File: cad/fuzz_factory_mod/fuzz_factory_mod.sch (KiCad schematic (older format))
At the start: 2 parts

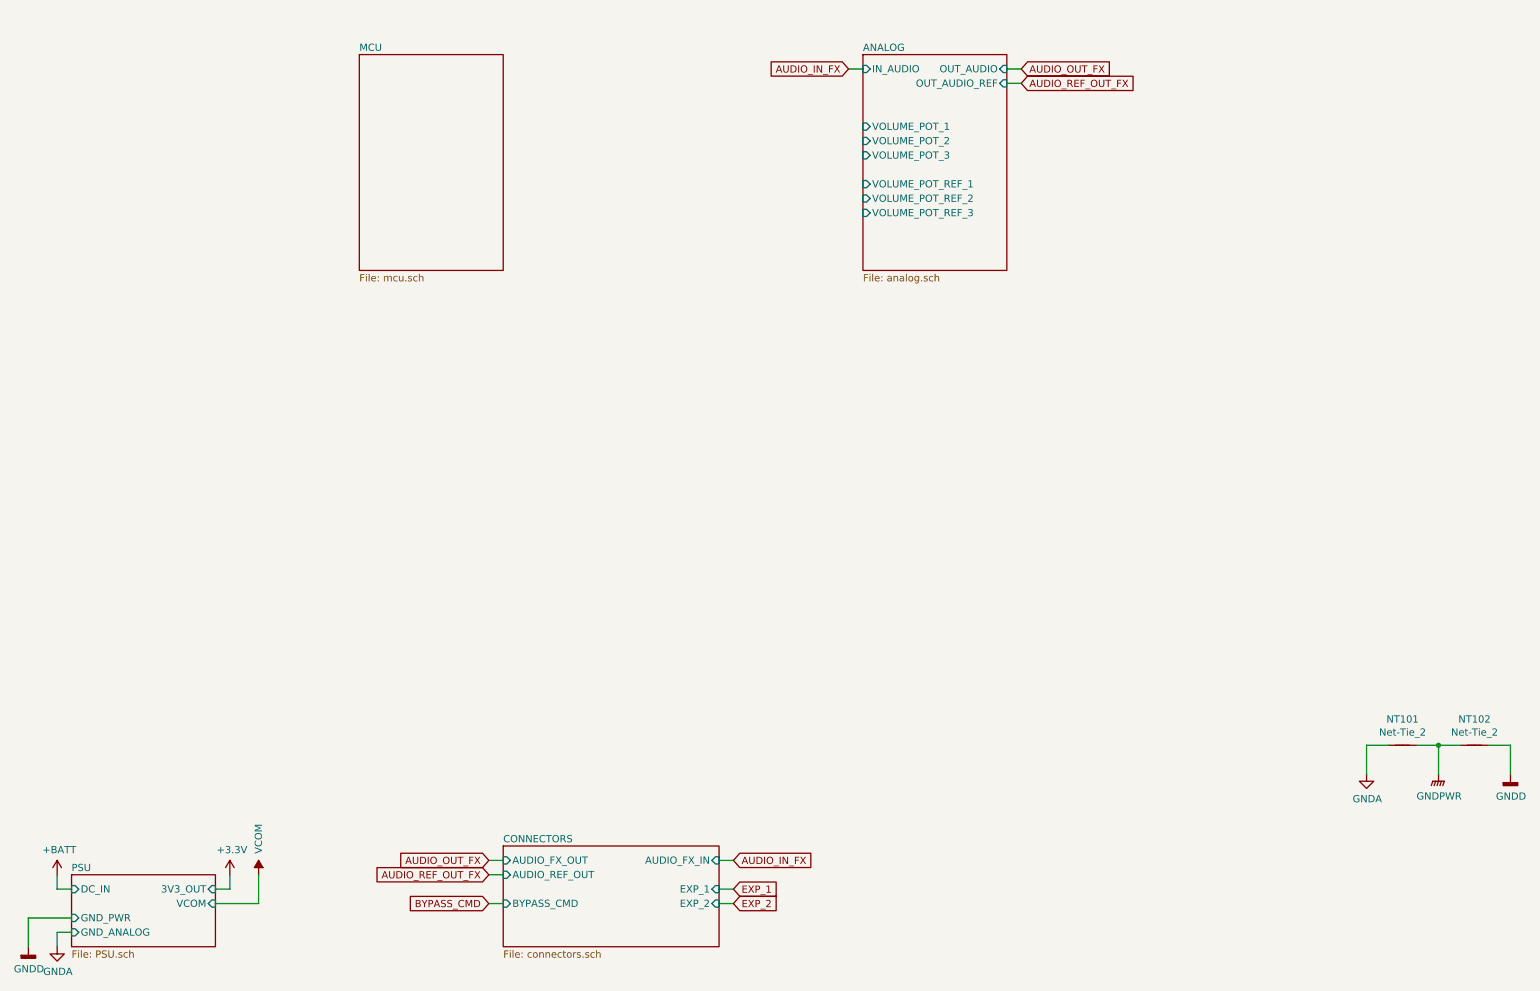
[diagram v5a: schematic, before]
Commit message: Changes architecture.
Corrections on schematic.
Continued Layout placement.
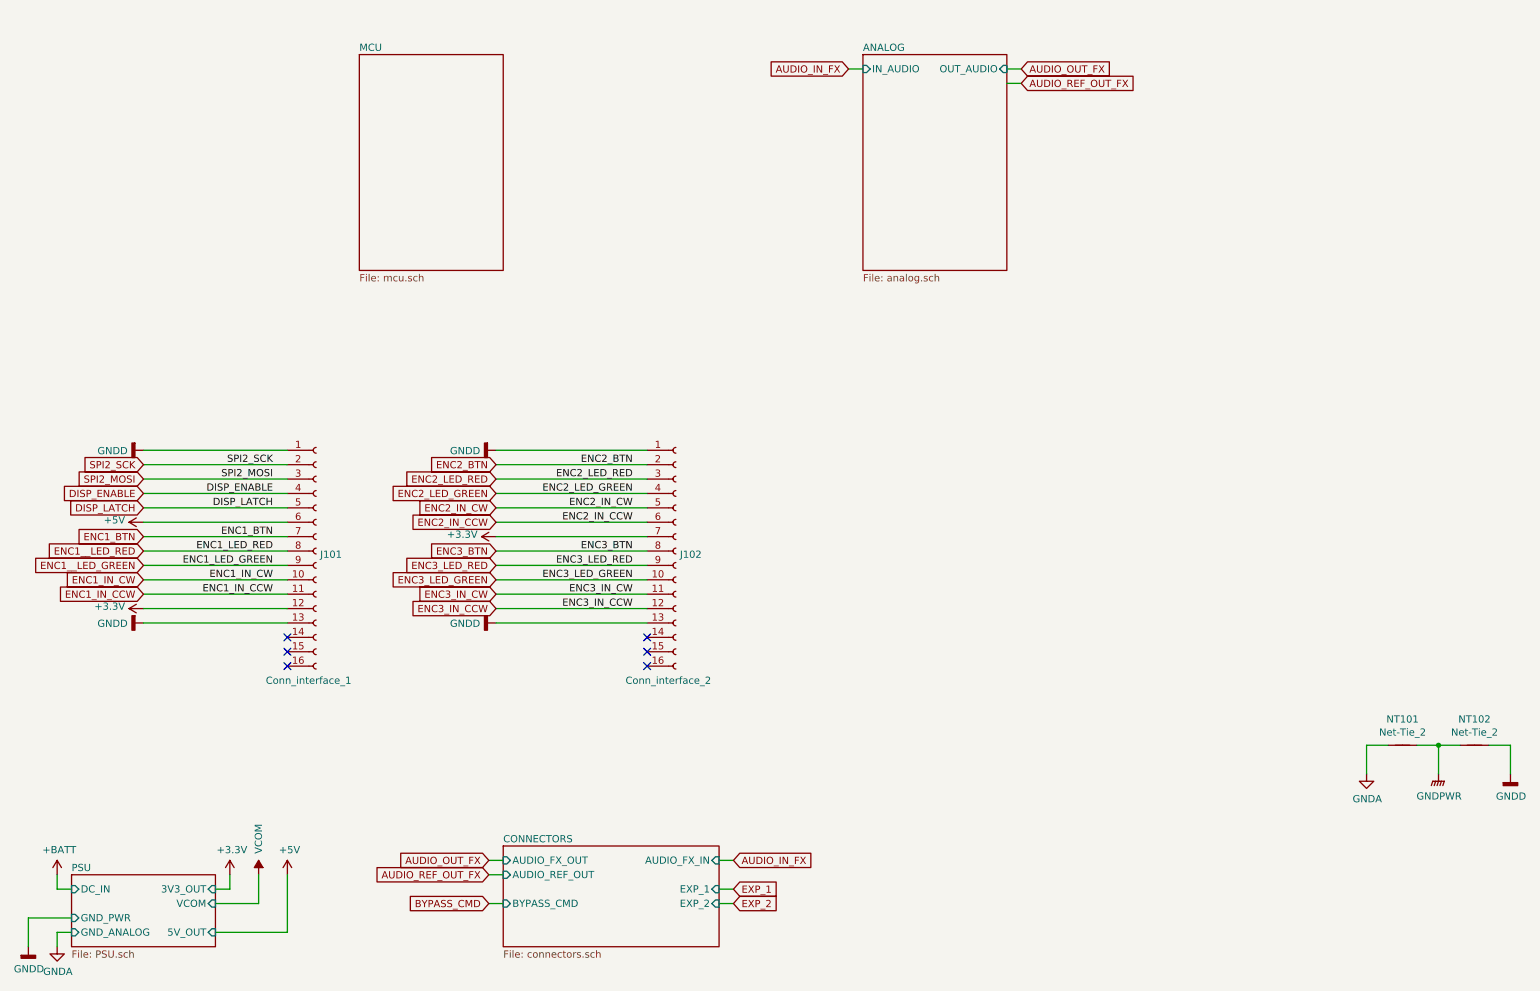
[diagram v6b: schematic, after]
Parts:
- added J101: Conn_interface_1, Pin_Headers:Pin_Header_Straight_1x16_Pitch2.54mm_SMD_Pin1Left, symbol Connector:Conn_01x16_Female
- added J102: Conn_interface_2, Pin_Headers:Pin_Header_Straight_1x16_Pitch2.54mm_SMD_Pin1Left, symbol Connector:Conn_01x16_Female
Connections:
- net +3V3: now also J101.12 (Pin_12), J102.7 (Pin_7)
- net GNDD: now also J101.1 (Pin_1), J101.13 (Pin_13), J102.1 (Pin_1), J102.13 (Pin_13)
- new net +5V: J101.6 (Pin_6)
- new net DISP_ENABLE: J101.4 (Pin_4)
- new net DISP_LATCH: J101.5 (Pin_5)
- new net ENC1_BTN: J101.7 (Pin_7)
- new net ENC1_IN_CCW: J101.11 (Pin_11)
- new net ENC1_IN_CW: J101.10 (Pin_10)
- new net ENC1__LED_GREEN: J101.9 (Pin_9)
- new net ENC1__LED_RED: J101.8 (Pin_8)
- new net ENC2_BTN: J102.2 (Pin_2)
- new net ENC2_IN_CCW: J102.6 (Pin_6)
- new net ENC2_IN_CW: J102.5 (Pin_5)
- new net ENC2_LED_GREEN: J102.4 (Pin_4)
- new net ENC2_LED_RED: J102.3 (Pin_3)
- new net ENC3_BTN: J102.8 (Pin_8)
- new net ENC3_IN_CCW: J102.12 (Pin_12)
- new net ENC3_IN_CW: J102.11 (Pin_11)
- new net ENC3_LED_GREEN: J102.10 (Pin_10)
- new net ENC3_LED_RED: J102.9 (Pin_9)
- new net SPI2_MOSI: J101.3 (Pin_3)
- new net SPI2_SCK: J101.2 (Pin_2)
- no-connect marks 0 -> 6

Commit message: Continued layout.
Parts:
- removed NT101, NT102: Net-Tie_2, Oddities:NetTie-II, symbol Device:Net-Tie_2
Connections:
- net GNDD is gone; now on net GNDA: J101.1 (Pin_1), J101.13 (Pin_13), J102.1 (Pin_1), J102.13 (Pin_13)
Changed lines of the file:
@@
-	1    0    0    -1
-$EndComp
-$Comp
-L Device:Net-Tie_2 NT101
-U 1 1 5E05BC9C
-P 10250 5800
-F 0 "NT101" H 10250 5981 50  0000 C CNN
-F 1 "Net-Tie_2" H 10250 5890 50  0000 C CNN
-F 2 "Oddities:NetTie-II" H 10250 5800 50  0001 C CNN
-F 3 "~" H 10250 5800 50  0001 C CNN
-	1    10250 5800
-	1    0    0    -1
-$EndComp
-$Comp
-L Device:Net-Tie_2 NT102
-U 1 1 5E05C2E4
-P 10750 5800
-F 0 "NT102" H 10750 5981 50  0000 C CNN
-F 1 "Net-Tie_2" H 10750 5890 50  0000 C CNN
-F 2 "Oddities:NetTie-II" H 10750 5800 50  0001 C CNN
-F 3 "~" H 10750 5800 50  0001 C CNN
-	1    10750 5800
 	1    0    0    -1
 $EndComp
 Wire Wire Line
 	11000 6000 11000 5800
-Wire Wire Line
-	11000 5800 10850 5800
-Wire Wire Line
-	10650 5800 10500 5800
 Wire Wire Line
 	10500 6000 10500 5800
 Connection ~ 10500 5800
 Wire Wire Line
-	10500 5800 10350 5800
-Wire Wire Line
 	10000 6000 10000 5800
-Wire Wire Line
-	10000 5800 10150 5800
 $Sheet
 S 1000 6700 1000 500
@@
 NoConn ~ 5000 5150
 NoConn ~ 5000 5250
+Wire Wire Line
+	10500 5800 11000 5800
+Wire Wire Line
+	10000 5800 10500 5800
 $EndSCHEMATC
